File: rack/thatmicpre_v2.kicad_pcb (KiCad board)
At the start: 2 copper layers, 140 x 73.4 mm, 89 parts, among them J1 CON-SOCJ-2155, J10 Angled pinheader, J2 NC3FBH2, J3 NC3MBH1, J4 Female header, J5 Male pinheader, J6 Female header, J7 Male pinheader, J8 Angled pinheader, J9 NMJ6HFD2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

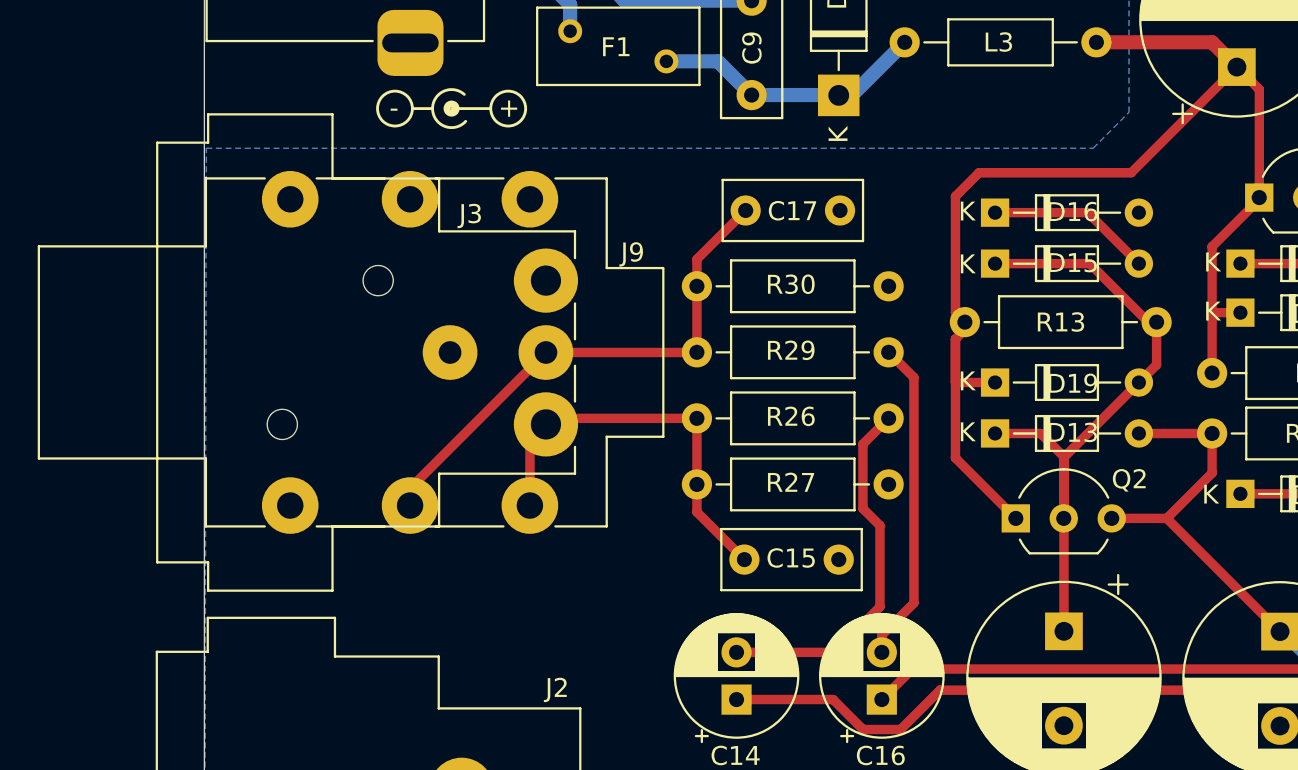
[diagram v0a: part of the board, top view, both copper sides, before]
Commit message: change NC3MBH1 to be NCJ6FA-H
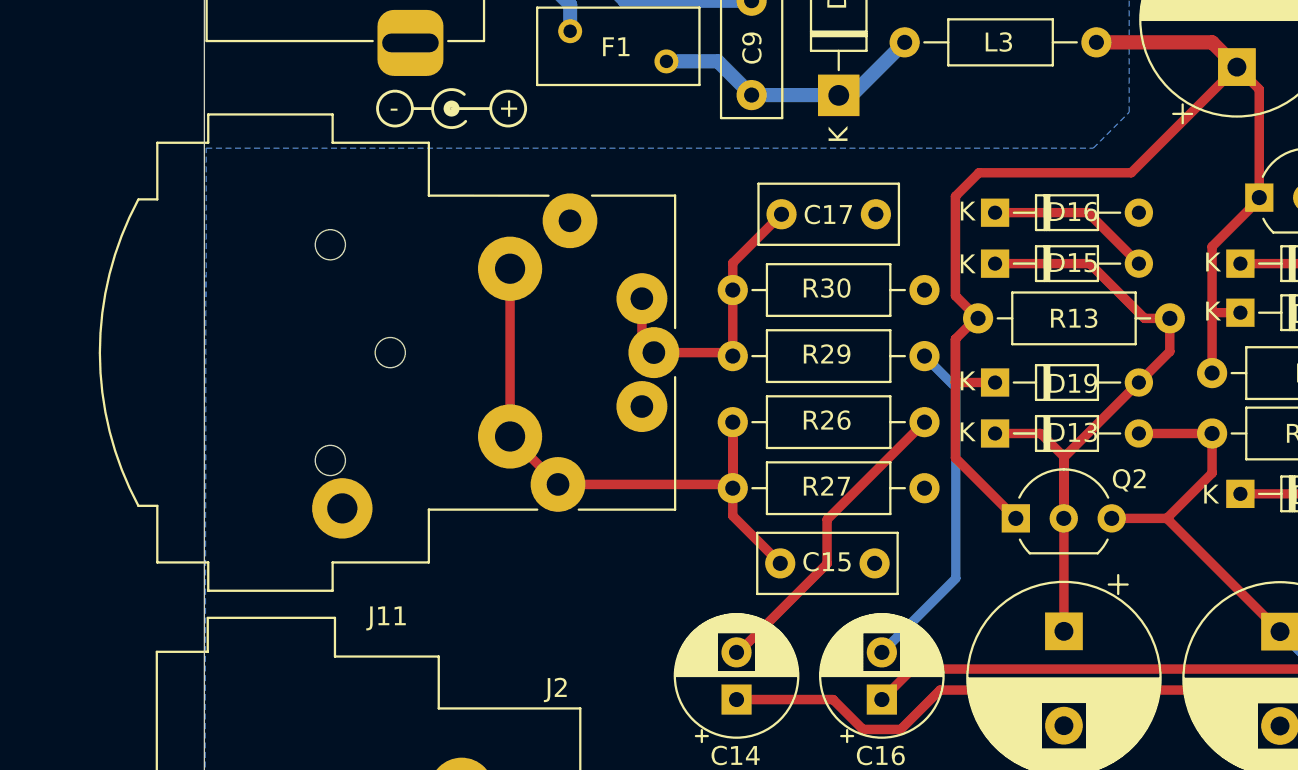
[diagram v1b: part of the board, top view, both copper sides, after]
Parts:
- removed J3: NC3MBH1, Connector_Audio:Jack_XLR_Neutrik_NC3MBH_Horizontal
- removed J9: NMJ6HFD2, Connector_Audio:Jack_6.35mm_Neutrik_NMJ6HFD2_Horizontal
- added J11: NCJ6FA-H, Connector_Audio:Jack_XLR-6.35mm_Neutrik_NCJ6FA-H_Horizontal, F.Cu at (99.2, 90.1)
- moved C15 1.91 mm to (111.0, 94.3)
- moved C17 1.91 mm to (111.1, 75.8)
- moved R26 1.91 mm to (108.5, 86.8)
- moved R27 1.91 mm to (108.5, 90.3)
- moved R29 1.91 mm to (108.5, 83.3)
- moved R30 1.91 mm to (108.5, 79.8)
- moved R13 0.73 mm to (121.5, 81.3)
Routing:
- net Net-(C15-Pad1): track 21.3 -> 33.9 mm
- net Net-(C17-Pad1): track 27.6 -> 16.2 mm
- net Net-(C14-Pad2): track 19.5 -> 16.4 mm
- net Net-(D13-K): track 35.7 -> 36.8 mm
- net Net-(C16-Pad2): track 17.2 -> 18.0 mm
- net /VIN: track 68.2 -> 68.8 mm

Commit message: Change diameter of GND pad  to be 5.2mm
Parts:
- removed H2, H3, H4: M3, MountingHole:MountingHole_3.2mm_M3_Pad
- added H1: M3, MountingHole:MountingHole_3.2mm_M3_Pad, F.Cu at (105.5, 121.4)
- added H1: M3, MountingHole:MountingHole_3.2mm_M3_Pad, F.Cu at (170.5, 59.4)
- added H1: M3, MountingHole:MountingHole_3.2mm_M3_Pad, F.Cu at (105.5, 59.4)

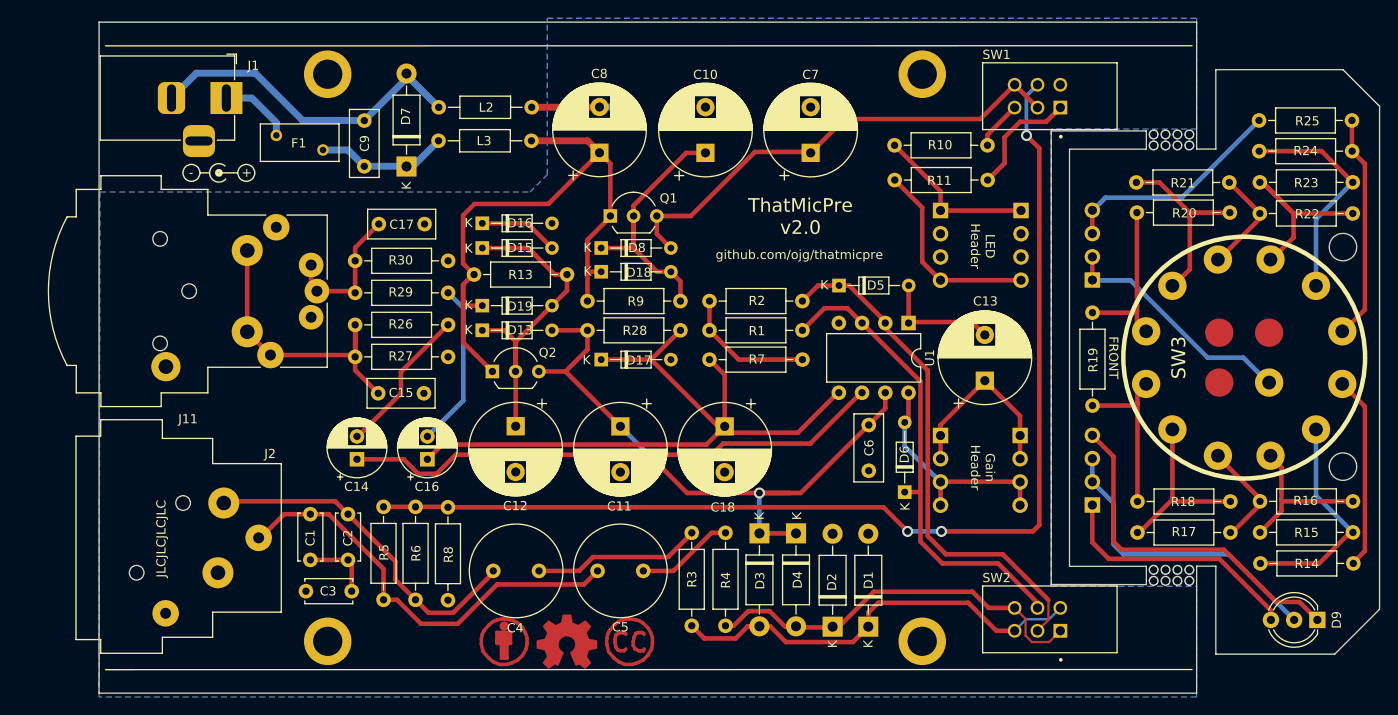
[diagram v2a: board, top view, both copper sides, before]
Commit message: Change motherboard width to be 73.6mm
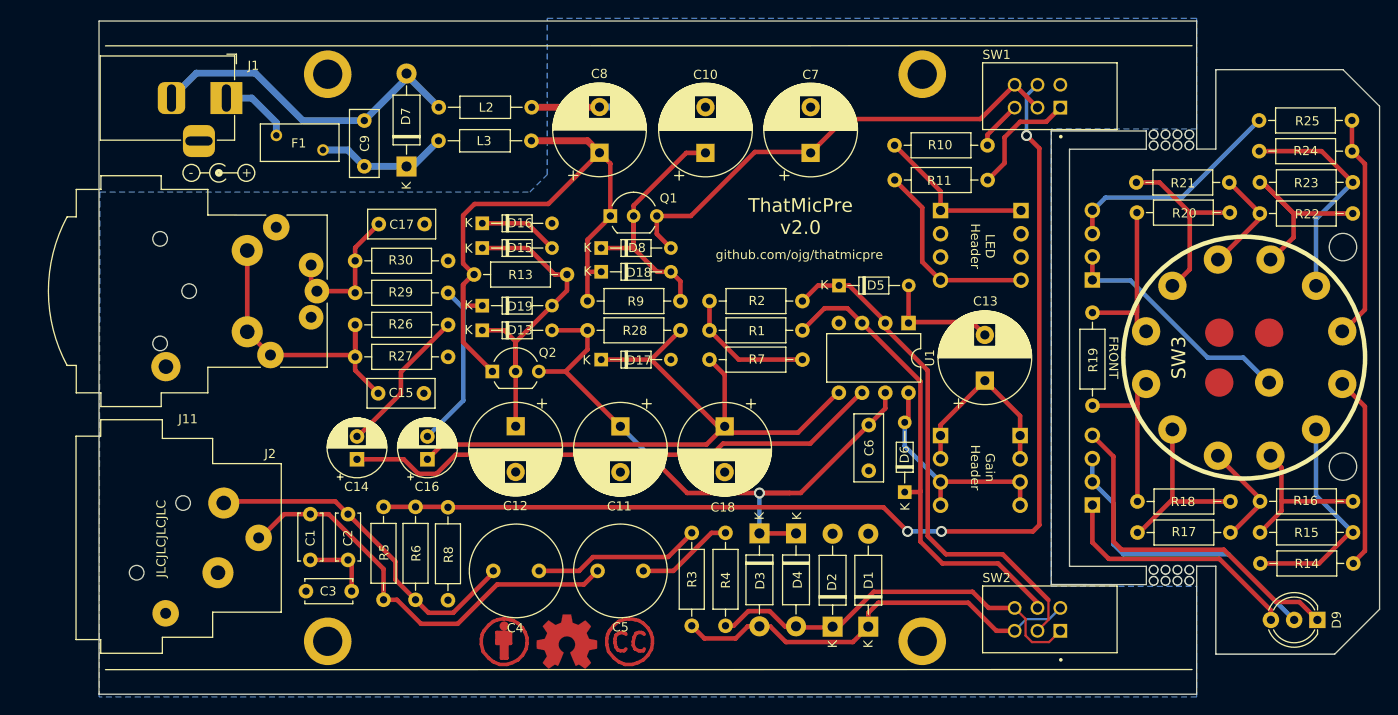
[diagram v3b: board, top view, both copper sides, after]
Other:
- board size 140 x 73.4 mm -> 140 x 73.6 mm
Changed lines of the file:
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@@
 	)
 	(gr_line
-		(start 80.5 53.7)
-		(end 80.5 127.068)
+		(start 80.5 53.584)
+		(end 80.5 127.184)
 		(stroke
 			(width 0.05)
@@
 	)
 	(gr_line
-		(start 200.5 127.068)
-		(end 80.5 127.068)
+		(start 200.5 127.184)
+		(end 80.5 127.184)
 		(stroke
 			(width 0.05)
@@
 	)
 	(gr_line
-		(start 200.5 53.7)
-		(end 80.5 53.7)
+		(start 200.5 53.584)
+		(end 80.5 53.584)
 		(stroke
 			(width 0.05)
@@
 	(gr_line
 		(start 200.5 67.584)
-		(end 200.5 53.7)
+		(end 200.5 53.584)
 		(stroke
 			(width 0.05)
@@
 	)
 	(gr_line
-		(start 200.5 127.068)
+		(start 200.5 127.184)
 		(end 200.5 113.184)
 		(stroke

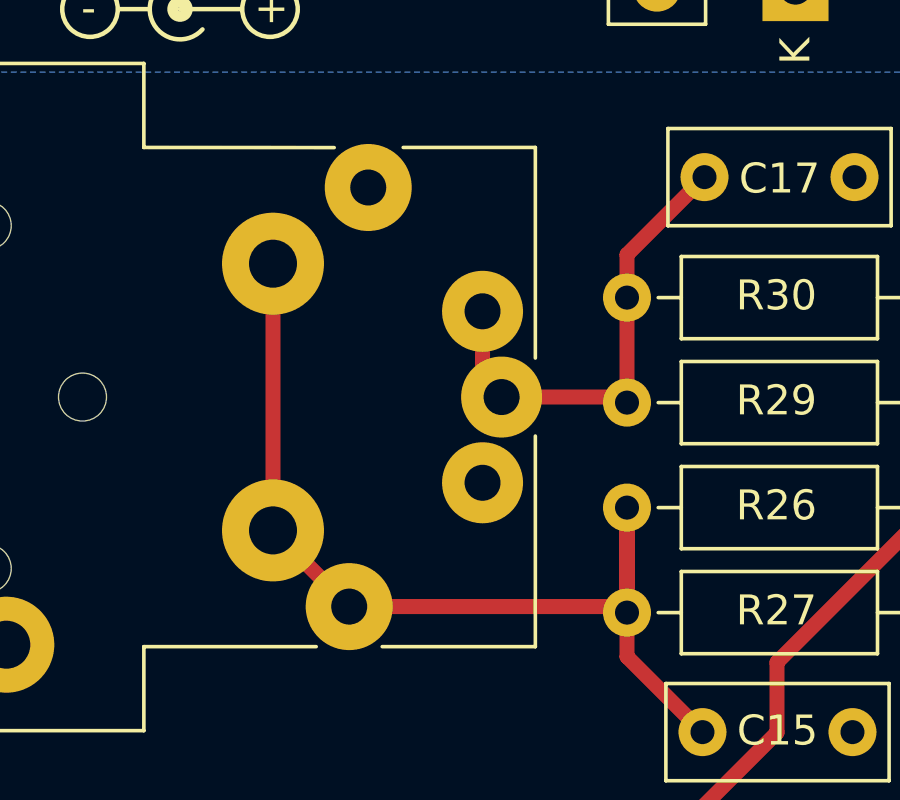
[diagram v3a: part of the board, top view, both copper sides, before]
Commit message: Fixed bug, NCJ6FA-H where 1-2pin connections were interchanged
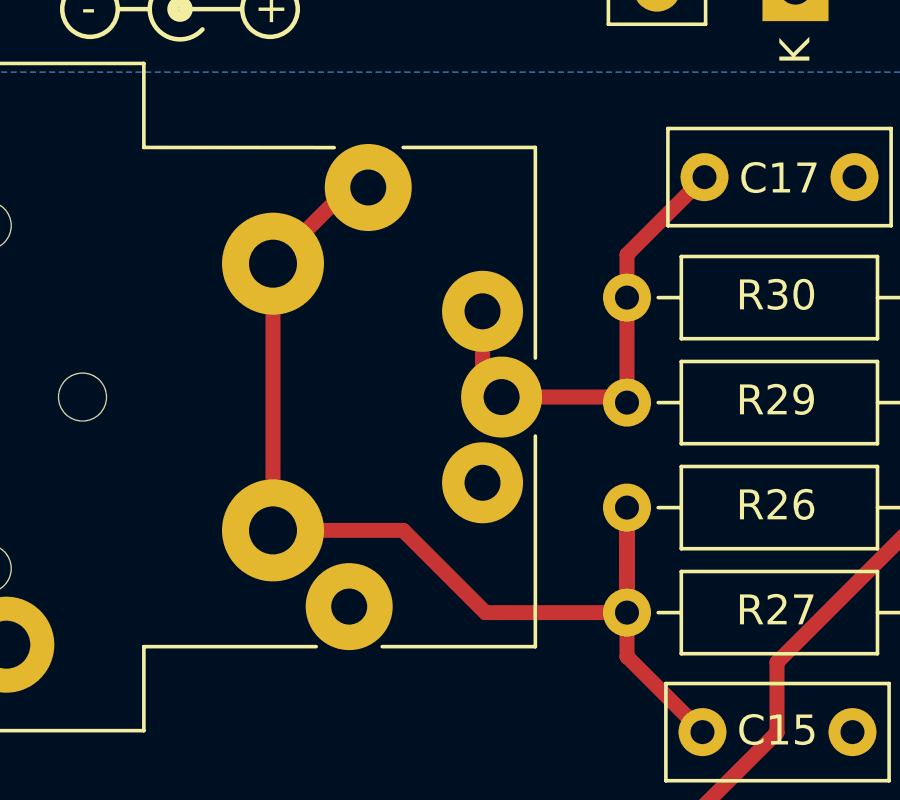
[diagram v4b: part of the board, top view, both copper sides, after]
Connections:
- J11 pad 1: Net-(C15-Pad1) -> GND
- J11 pad 2: GND -> Net-(C15-Pad1)
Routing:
- net Net-(C15-Pad1): track 33.9 -> 38.2 mm
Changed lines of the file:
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@@
 			(layers "*.Cu" "*.Mask")
 			(remove_unused_layers no)
-			(net 38 "Net-(C15-Pad1)")
+			(net 3 "GND")
 			(pintype "passive")
 		)
@@
 			(layers "*.Cu" "*.Mask")
 			(remove_unused_layers no)
-			(net 3 "GND")
+			(net 38 "Net-(C15-Pad1)")
 			(pintype "passive")
 		)
@@
 	)
 	(segment
+		(start 101.044 87.56)
+		(end 96.7 87.56)
+		(width 0.5)
+		(layer "F.Cu")
+		(net 38)
+	)
+	(segment
 		(start 108.5 91.768)
 		(end 111.016 94.284)
@@
 	)
 	(segment
+		(start 99.875 76.13)
+		(end 99.24 76.13)
+		(width 0.5)
+		(layer "F.Cu")
+		(net 38)
+	)
+	(segment
 		(start 96.7 78.67)
 		(end 96.7 87.56)
@@
 	)
 	(segment
-		(start 108.5 90.1)
-		(end 99.24 90.1)
+		(start 108.5 90.3)
+		(end 108.5 91.768)
 		(width 0.5)
 		(layer "F.Cu")
@@
 	)
 	(segment
-		(start 108.5 90.3)
-		(end 108.5 91.768)
+		(start 99.24 76.13)
+		(end 96.7 78.67)
 		(width 0.5)
 		(layer "F.Cu")
@@
 	)
 	(segment
-		(start 96.7 87.56)
-		(end 99.24 90.1)
+		(start 103.784 90.3)
+		(end 101.044 87.56)
 		(width 0.5)
 		(layer "F.Cu")
@@
 		(width 0.5)
 		(layer "F.Cu")
+		(net 38)
+	)
+	(segment
+		(start 108.5 90.3)
+		(end 103.784 90.3)
+		(width 0.5)
+		(layer "F.Cu")

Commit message: Modify the footprints of 0.5W and 1W resistors
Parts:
- R3, R4: footprint Resistor_THT:R_Axial_DIN0207_L6.3mm_D2.5mm_P10.16mm_Horizontal -> Resistor_THT:R_Axial_DIN0411_L9.9mm_D3.6mm_P15.24mm_Horizontal
- R5, R6: footprint Resistor_THT:R_Axial_DIN0207_L6.3mm_D2.5mm_P10.16mm_Horizontal -> Resistor_THT:R_Axial_DIN0309_L9.0mm_D3.2mm_P12.70mm_Horizontal
- moved R4 6.37 mm to (145.0, 124.7)
- moved R3 6.17 mm to (149.0, 124.7)
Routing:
- net Net-(C4-Pad2): track 18.5 -> 29.5 mm
- net Net-(D2-K): track 43.5 -> 51.3 mm
- net Net-(C1-Pad1): track 47.5 -> 50.6 mm
- net Net-(C2-Pad1): track 37.8 -> 40.7 mm
- net Net-(C5-Pad2): track 10.7 -> 8.17 mm
- net Net-(D1-K): track 47.1 -> 45.6 mm
